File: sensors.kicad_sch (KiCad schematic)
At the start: 8 parts

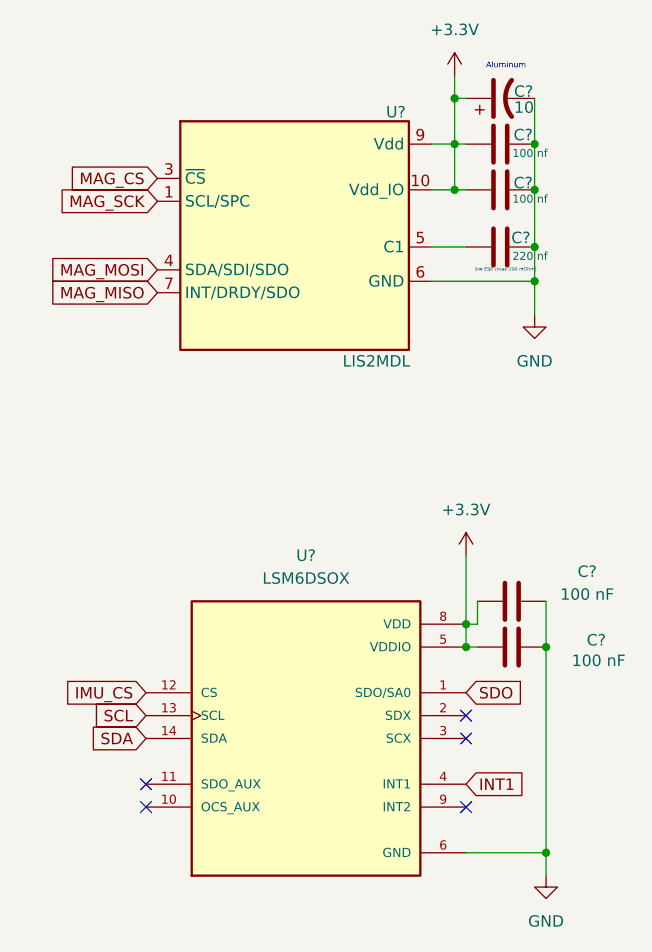
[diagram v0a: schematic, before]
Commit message: Changed the wording of the labels to fit SPI
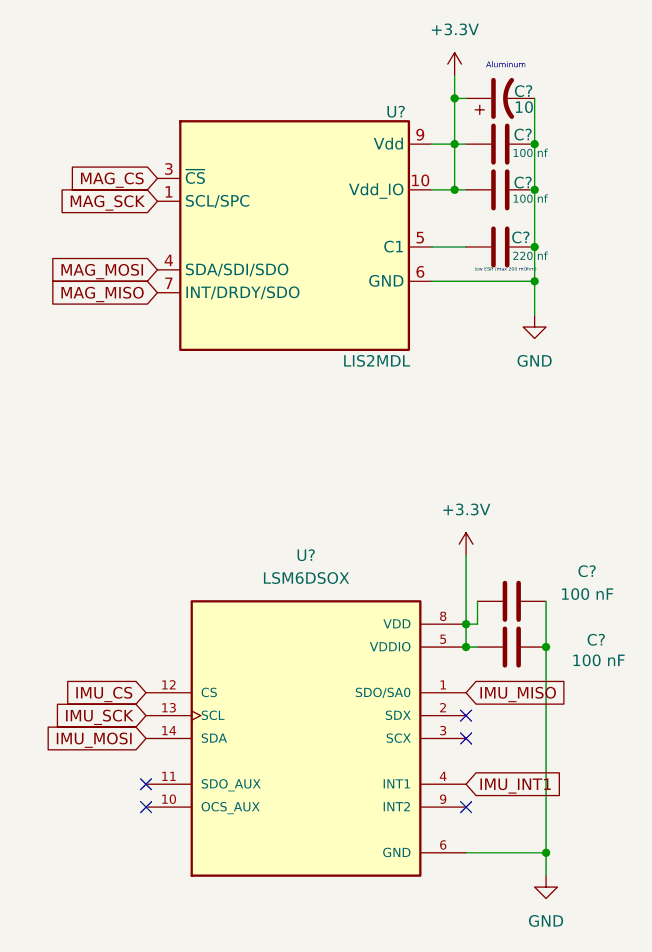
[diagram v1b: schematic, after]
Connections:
- net INT1 renamed IMU_INT1
- net SCL renamed IMU_SCK
- net SDA renamed IMU_MOSI
- net SDO renamed IMU_MISO
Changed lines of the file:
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@@
 		)
 	)
-	(global_label "INT1"
+	(global_label "IMU_INT1"
 		(shape input)
 		(at 83.82 110.49 0)
@@
 		)
 		(property "Intersheetrefs" "${INTERSHEET_REFS}"
-			(at 90.9176 110.49 0)
+			(at 95.2719 110.49 0)
 			(effects
 				(font
@@
 		)
 	)
-	(global_label "SDA"
+	(global_label "IMU_MOSI"
 		(shape input)
 		(at 48.26 105.41 180)
@@
 		)
 		(property "Intersheetrefs" "${INTERSHEET_REFS}"
-			(at 41.7067 105.41 0)
+			(at 36.3243 105.41 0)
 			(effects
 				(font
@@
 		)
 	)
-	(global_label "SDO"
+	(global_label "IMU_MISO"
 		(shape input)
 		(at 83.82 100.33 0)
@@
 		)
 		(property "Intersheetrefs" "${INTERSHEET_REFS}"
-			(at 90.6152 100.33 0)
+			(at 95.7557 100.33 0)
 			(effects
 				(font
@@
 		)
 	)
-	(global_label "SCL"
+	(global_label "IMU_SCK"
 		(shape input)
 		(at 48.26 102.87 180)
@@
 		)
 		(property "Intersheetrefs" "${INTERSHEET_REFS}"
-			(at 41.7672 102.87 0)
+			(at 37.171 102.87 0)
 			(effects
 				(font
